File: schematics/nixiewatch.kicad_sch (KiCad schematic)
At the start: 33 parts, among them Q1 BC546, Q2 6N90C, Q3 BC546, U1 NE555P, U2 TPIC6B595, U3 MCP1702-5002E/TO, U4 TPIC6B595, U5 TPIC6B595, U6 ATtiny45V-10P

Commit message: update
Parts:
- removed C2: 330u, Capacitor_THT:CP_Radial_D8.0mm_P3.50mm, symbol Device:C_Polarized_Small
- removed C3: 100p, Capacitor_THT:C_Disc_D3.0mm_W2.0mm_P2.50mm, symbol Device:C_Small
- removed D1: 200V, Diode_THT:D_A-405_P12.70mm_Horizontal, symbol Device:D
- removed R6: 2k2, Resistor_THT:R_Axial_DIN0207_L6.3mm_D2.5mm_P7.62mm_Horizontal, symbol Device:R_Small
- added C2: 100n, Capacitor_THT:C_Disc_D3.0mm_W2.0mm_P2.50mm, symbol Device:C_Small
- added D1: 1N4007, Diode_THT:D_DO-41_SOD81_P10.16mm_Horizontal, symbol Diode:1N4007
- C4: value 4u7 400V -> 1u 200V
- Q2: value 6N90C -> BXP2N65
- R7: value 640k -> 680k
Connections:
- net +170V: now also D1.1 (K)
- net GND: now also C2.2
- net at R13.2, U2.13 (SRCK), U4.13 (SRCK)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: now also U6.3 (XTAL2/PB4); no longer U6.6 (PB1)
- net at U2.3 (SER_IN): now also U6.2 (XTAL1/PB3); no longer U6.5 (AREF/PB0)
- net at L1.2, Q2.2 (D): now also D1.2 (A)

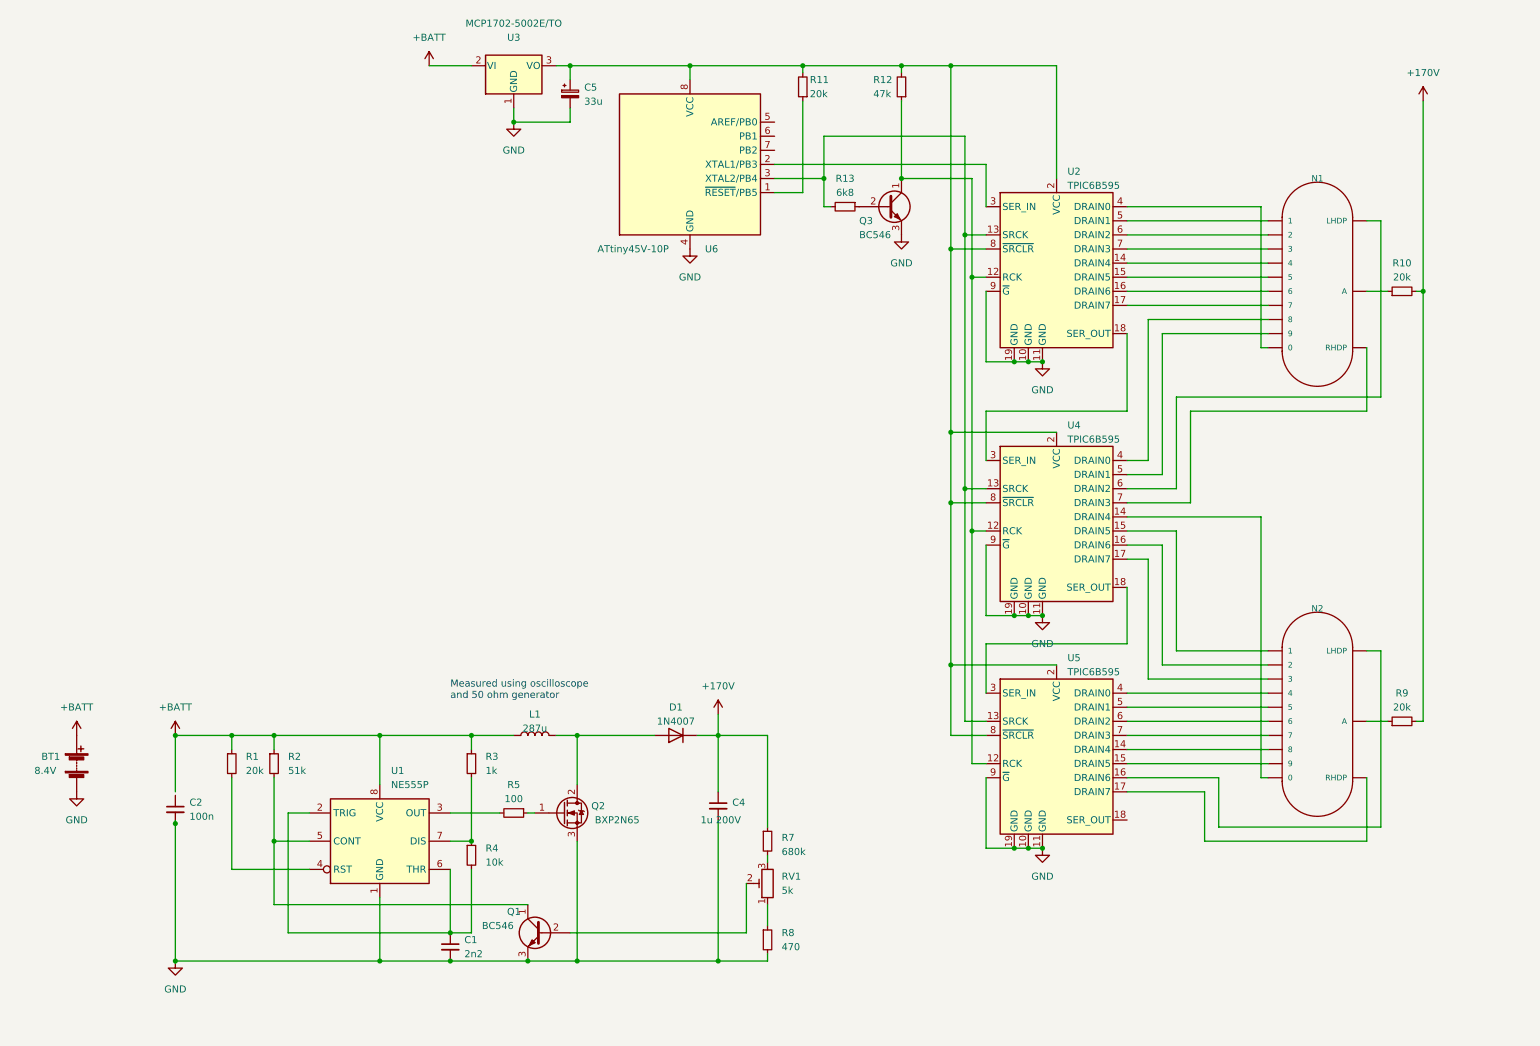
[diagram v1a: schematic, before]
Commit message: allow user to set time
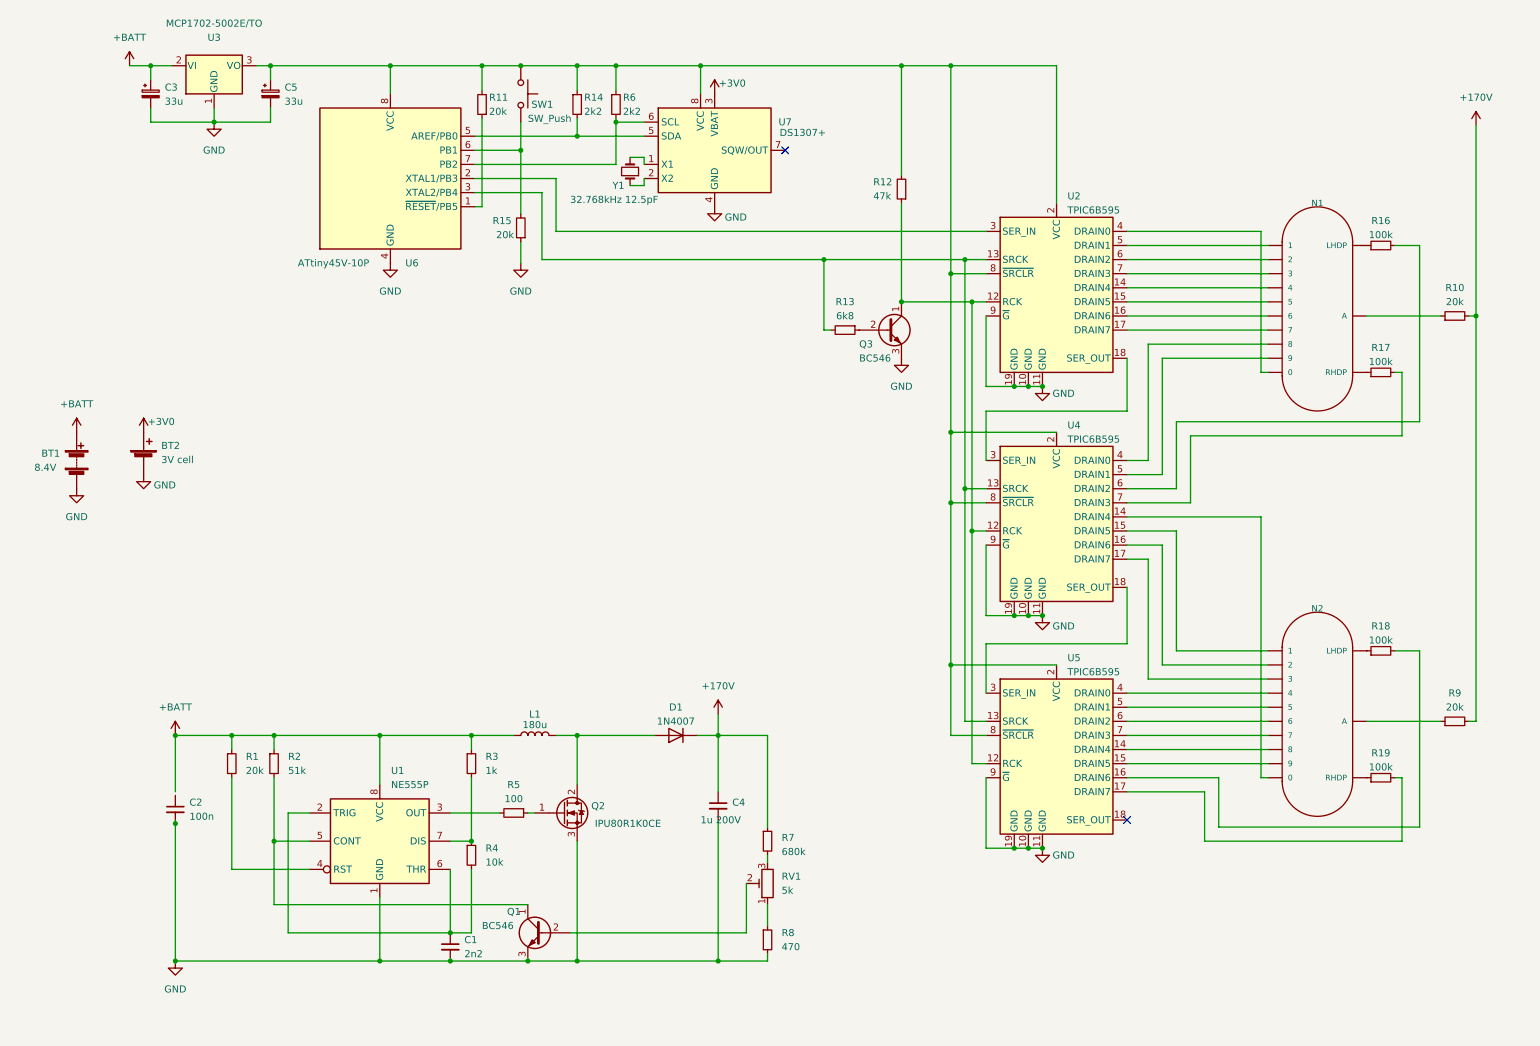
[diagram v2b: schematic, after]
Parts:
- added BT2: 3V cell, symbol Device:Battery_Cell
- added C3: 33u, symbol Device:C_Polarized_Small
- added R14, R6: 2k2, symbol Device:R_Small
- added R15: 20k, symbol Device:R_Small
- added R16, R17, R18, R19: 100k, symbol Device:R_Small
- added SW1: SW_Push, symbol Switch:SW_Push
- added U7: DS1307+, Package_DIP:DIP-8_W7.62mm, symbol Timer_RTC:DS1307+
- added Y1: 32.768kHz 12.5pF, symbol Device:Crystal_Small
- L1: value 287u -> 180u
- Q2: value BXP2N65 -> IPU80R1K0CE
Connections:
- net +BATT: now also C3.1
- net GND: now also BT2.2 (-), C3.2, R15.1, U7.4 (GND)
- net at C5.1, R11.2, R12.2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: now also R14.1, R6.1, SW1.1, U7.8 (VCC)
- net at U4.6 (DRAIN2): now also R16.2; no longer N1.LHDP
- net at U4.7 (DRAIN3): now also R17.2; no longer N1.RHDP
- net at U5.16 (DRAIN6): now also R18.2; no longer N2.LHDP
- net at U5.17 (DRAIN7): now also R19.2; no longer N2.RHDP
- net at U6.5 (AREF/PB0): now also R14.2, U7.5 (SDA)
- net at U6.6 (PB1): now also R15.2, SW1.2
- net at U6.7 (PB2): now also R6.2, U7.6 (SCL)
- new net: U7.1 (X1), Y1.2
- new net: U7.2 (X2), Y1.1
- new net: N2.LHDP, R18.1
- new net: N2.RHDP, R19.1
- new net: N1.LHDP, R16.1
- new net: N1.RHDP, R17.1
- new net +3V0: BT2.1 (+), U7.3 (VBAT)
- no-connect marks 0 -> 2
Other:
- note removed: "Measured using oscilloscope and 50 ohm generator"
- moved on the sheet: BT1, C5, N1, Q3, R10, R11, R12, R13, R9, U2, U3, U6

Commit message: pcb layout
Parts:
- BT1: footprint (none) -> Connector_PinHeader_2.00mm:PinHeader_1x01_P2.00mm_Vertical
- BT2: value 3V cell -> 3V; footprint (none) -> Connector_PinHeader_2.00mm:PinHeader_1x01_P2.00mm_Vertical
- C3, C5: footprint (none) -> Capacitor_THT:CP_Radial_D4.0mm_P1.50mm
- C4: footprint Capacitor_THT:CP_Radial_D8.0mm_P3.50mm -> Capacitor_THT:CP_Radial_D5.0mm_P2.50mm
- L1: footprint Inductor_THT:L_Toroid_Horizontal_D21.8mm_P19.60mm_Bourns_2100 -> Inductor_THT:L_Radial_D12.0mm_P5.00mm_Neosid_SD12k_style2
- N1, N2: footprint nixies-us_IN-16 -> Connector_PinHeader_2.00mm:PinHeader_1x13_P2.00mm_Vertical
- Q2: footprint Package_TO_SOT_THT:TO-220F-3_Horizontal_TabDown -> Package_TO_SOT_THT:SIPAK-1EP_Horizontal_TabDown
- R10, R11, R12, R13, R14, R15, R16, R17, R18, R19, R6, R9: footprint (none) -> Resistor_THT:R_Axial_DIN0207_L6.3mm_D2.5mm_P7.62mm_Horizontal
- SW1: footprint (none) -> Connector_Pin:Pin_D0.7mm_L6.5mm_W1.8mm_FlatFork
- U2, U4, U5: footprint (none) -> Package_DIP:DIP-20_W7.62mm
- Y1: footprint (none) -> Crystal:Crystal_C38-LF_D3.0mm_L8.0mm_Horizontal
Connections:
- net +BATT: now also C2.1
- net at U7.1 (X1): now also Y1.1; no longer Y1.2
- net at U7.2 (X2): now also Y1.2; no longer Y1.1
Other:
- moved on the sheet: Y1
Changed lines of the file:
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@@
+    (stroke (width 0) (type default))
+  )
+  (wire (pts (xy 125.095 43.18) (xy 125.095 41.91))
     (stroke (width 0) (type default))
   )
@@
     (stroke (width 0) (type default))
   )
-  (wire (pts (xy 125.095 41.91) (xy 125.095 43.18))
+  (wire (pts (xy 121.92 43.18) (xy 125.095 43.18))
     (stroke (width 0) (type default))
   )
@@
     (stroke (width 0) (type default))
   )
+  (wire (pts (xy 125.095 39.37) (xy 125.095 38.1))
+    (stroke (width 0) (type default))
+  )
   (wire (pts (xy 228.6 158.75) (xy 264.795 158.75))
     (stroke (width 0) (type default))
@@
     (stroke (width 0) (type default))
   )
-  (wire (pts (xy 122.555 38.1) (xy 125.095 38.1))
-    (stroke (width 0) (type default))
-  )
   (wire (pts (xy 113.03 34.29) (xy 125.095 34.29))
     (stroke (width 0) (type default))
@@
     (stroke (width 0) (type default))
   )
-  (wire (pts (xy 125.095 38.1) (xy 125.095 39.37))
-    (stroke (width 0) (type default))
-  )
   (wire (pts (xy 120.015 21.59) (xy 135.255 21.59))
     (stroke (width 0) (type default))
@@
     (stroke (width 0) (type default))
   )
-  (wire (pts (xy 122.555 43.18) (xy 125.095 43.18))
-    (stroke (width 0) (type default))
-  )
   (wire (pts (xy 94.615 36.83) (xy 102.87 36.83))
     (stroke (width 0) (type default))
@@
     (stroke (width 0) (type default))
   )
+  (wire (pts (xy 125.095 38.1) (xy 121.92 38.1))
+    (stroke (width 0) (type default))
+  )
   (wire (pts (xy 180.34 21.59) (xy 180.34 59.055))
     (stroke (width 0) (type default))
@@
     (stroke (width 0) (type default))
   )
-  (wire (pts (xy 40.64 142.24) (xy 40.64 152.4))
+  (wire (pts (xy 40.64 142.24) (xy 40.64 153.035))
     (stroke (width 0) (type default))
   )
@@
       (effects (font (size 1.27 1.27)) (justify left))
     )
-    (property "Footprint" "" (at 107.95 26.67 0)
+    (property "Footprint" "Connector_Pin:Pin_D0.7mm_L6.5mm_W1.8mm_FlatFork" (at 107.95 26.67 0)
       (effects (font (size 1.27 1.27)) hide)
     )
@@
       (effects (font (size 1.27 1.27)) (justify left))
     )
-    (property "Footprint" "" (at 215.9 119.38 0)
+    (property "Footprint" "Package_DIP:DIP-20_W7.62mm" (at 215.9 119.38 0)
       (effects (font (size 1.27 1.27)) hide)
     )
@@
       (effects (font (size 1.27 1.27)) (justify left))
     )
-    (property "Footprint" "" (at 215.9 161.29 0)
+    (property "Footprint" "Package_DIP:DIP-20_W7.62mm" (at 215.9 161.29 0)
       (effects (font (size 1.27 1.27)) hide)
     )
@@
       (effects (font (size 1.27 1.27)) (justify left))
     )
-    (property "Footprint" "" (at 215.9 78.105 0)
+    (property "Footprint" "Package_DIP:DIP-20_W7.62mm" (at 215.9 78.105 0)
       (effects (font (size 1.27 1.27)) hide)
     )
@@
       (effects (font (size 1.27 1.27)) (justify right))
     )
-    (property "Footprint" "" (at 95.885 28.575 0)
+    (property "Footprint" "Resistor_THT:R_Axial_DIN0207_L6.3mm_D2.5mm_P7.62mm_Horizontal" (at 95.885 28.575 0)
       (effects (font (size 1.27 1.27)) hide)
     )
@@
       (effects (font (size 1.27 1.27)) (justify left))
     )
-    (property "Footprint" "" (at 36.195 26.67 0)
+    (property "Footprint" "Capacitor_THT:CP_Radial_D4.0mm_P1.50mm" (at 36.195 26.67 0)
       (effects (font (size 1.27 1.27)) hide)
     )
@@
       (effects (font (size 1.27 1.27)))
     )
-    (property "Footprint" "" (at 271.145 66.675 0)
+    (property "Footprint" "Resistor_THT:R_Axial_DIN0207_L6.3mm_D2.5mm_P7.62mm_Horizontal" (at 271.145 66.675 0)
       (effects (font (size 1.27 1.27)) hide)
     )
@@
       (effects (font (size 1.27 1.27)) (justify left))
     )
-    (property "Footprint" "" (at 57.785 26.67 0)
+    (property "Footprint" "Capacitor_THT:CP_Radial_D4.0mm_P1.50mm" (at 57.785 26.67 0)
       (effects (font (size 1.27 1.27)) hide)
     )
@@
       (effects (font (size 1.27 1.27)) (justify left))
     )
-    (property "Value" "3V cell" (at 38.1 92.583 0)
-      (effects (font (size 1.27 1.27)) (justify left))
-    )
-    (property "Footprint" "" (at 34.925 91.186 90)
+    (property "Value" "3V" (at 38.1 92.583 0)
+      (effects (font (size 1.27 1.27)) (justify left))
+    )
+    (property "Footprint" "Connector_PinHeader_2.00mm:PinHeader_1x01_P2.00mm_Vertical" (at 34.925 91.186 90)
       (effects (font (size 1.27 1.27)) hide)
     )
@@
       (effects (font (size 1.27 1.27)))
     )
-    (property "Footprint" "" (at 257.81 127 0)
+    (property "Footprint" "Resistor_THT:R_Axial_DIN0207_L6.3mm_D2.5mm_P7.62mm_Horizontal" (at 257.81 127 0)
       (effects (font (size 1.27 1.27)) hide)
     )
@@
       (effects (font (size 1.27 1.27)))
     )
-    (property "Footprint" "" (at 257.81 149.86 0)
+    (property "Footprint" "Resistor_THT:R_Axial_DIN0207_L6.3mm_D2.5mm_P7.62mm_Horizontal" (at 257.81 149.86 0)
       (effects (font (size 1.27 1.27)) hide)
     )
@@
     )
   )
-  (symbol (lib_id "Device:Crystal_Small") (at 122.555 40.64 90) (unit 1)
-    (in_bom yes) (on_board yes) (dnp no)
-    (property "Reference" "Y1" (at 119.38 43.18 90)
+  (symbol (lib_id "Device:Crystal_Small") (at 121.92 40.64 270) (unit 1)
+    (in_bom yes) (on_board yes) (dnp no)
+    (property "Reference" "Y1" (at 121.285 43.18 90)
       (effects (font (size 1.27 1.27)) (justify right))
     )
-    (property "Value" "32.768kHz 12.5pF" (at 111.76 45.72 90)
+    (property "Value" "32.768kHz 12.5pF" (at 130.175 45.72 90)
       (effects (font (size 1.27 1.27)) (justify right))
     )
-    (property "Footprint" "" (at 122.555 40.64 0)
-      (effects (font (size 1.27 1.27)) hide)
-    )
-    (property "Datasheet" "~" (at 122.555 40.64 0)
+    (property "Footprint" "Crystal:Crystal_C38-LF_D3.0mm_L8.0mm_Horizontal" (at 121.92 40.64 0)
+      (effects (font (size 1.27 1.27)) hide)
+    )
+    (property "Datasheet" "~" (at 121.92 40.64 0)
       (effects (font (size 1.27 1.27)) hide)
     )
@@
       (effects (font (size 1.27 1.27)) (justify left))
     )
-    (property "Footprint" "" (at 22.86 91.186 90)
+    (property "Footprint" "Connector_PinHeader_2.00mm:PinHeader_1x01_P2.00mm_Vertical" (at 22.86 91.186 90)
       (effects (font (size 1.27 1.27)) hide)
     )
@@
       (effects (font (size 1.27 1.27)) (justify left))
     )
-    (property "Footprint" "Capacitor_THT:CP_Radial_D8.0mm_P3.50mm" (at 138.43 154.94 0)
+    (property "Footprint" "Capacitor_THT:CP_Radial_D5.0mm_P2.50mm" (at 138.43 154.94 0)
       (effects (font (size 1.27 1.27)) hide)
     )
@@
       (effects (font (size 1.27 1.27)) (justify left))
     )
-    (property "Footprint" "Package_TO_SOT_THT:TO-220F-3_Horizontal_TabDown" (at 115.57 153.67 0)
+    (property "Footprint" "Package_TO_SOT_THT:SIPAK-1EP_Horizontal_TabDown" (at 115.57 153.67 0)
       (effects (font (size 1.27 1.27)) hide)
     )
@@
       (effects (font (size 1.27 1.27)))
     )
-    (property "Footprint" "" (at 161.29 69.215 0)
+    (property "Footprint" "Resistor_THT:R_Axial_DIN0207_L6.3mm_D2.5mm_P7.62mm_Horizontal" (at 161.29 69.215 0)
       (effects (font (size 1.27 1.27)) hide)
     )
@@
       (effects (font (size 1.27 1.27)) (justify left))
     )
-    (property "Footprint" "" (at 120.015 28.575 0)
+    (property "Footprint" "Resistor_THT:R_Axial_DIN0207_L6.3mm_D2.5mm_P7.62mm_Horizontal" (at 120.015 28.575 0)
       (effects (font (size 1.27 1.27)) hide)
     )
@@
       (effects (font (size 1.27 1.27)))
     )
-    (property "Footprint" "Inductor_THT:L_Toroid_Horizontal_D21.8mm_P19.60mm_Bourns_2100" (at 105.41 142.24 0)
+    (property "Footprint" "Inductor_THT:L_Radial_D12.0mm_P5.00mm_Neosid_SD12k_style2" (at 105.41 142.24 0)
       (effects (font (size 1.27 1.27)) hide)
     )
@@
       (effects (font (size 1.27 1.27)))
     )
-    (property "Footprint" "" (at 257.81 53.975 0)
+    (property "Footprint" "Resistor_THT:R_Axial_DIN0207_L6.3mm_D2.5mm_P7.62mm_Horizontal" (at 257.81 53.975 0)
       (effects (font (size 1.27 1.27)) hide)
     )
@@
       (effects (font (size 1.27 1.27)) (justify right))
     )
-    (property "Footprint" "" (at 171.45 43.815 0)
+    (property "Footprint" "Resistor_THT:R_Axial_DIN0207_L6.3mm_D2.5mm_P7.62mm_Horizontal" (at 171.45 43.815 0)
       (effects (font (size 1.27 1.27)) hide)
     )
@@
       (effects (font (size 1.27 1.27)) (justify left))
     )
-    (property "Footprint" "" (at 113.03 28.575 0)
+    (property "Footprint" "Resistor_THT:R_Axial_DIN0207_L6.3mm_D2.5mm_P7.62mm_Horizontal" (at 113.03 28.575 0)
       (effects (font (size 1.27 1.27)) hide)
     )
@@
       (effects (font (size 1.27 1.27)))
     )
-    (property "Footprint" "" (at 271.145 139.7 0)
+    (property "Footprint" "Resistor_THT:R_Axial_DIN0207_L6.3mm_D2.5mm_P7.62mm_Horizontal" (at 271.145 139.7 0)
       (effects (font (size 1.27 1.27)) hide)
     )
@@
       (effects (font (size 1.143 1.143)) (justify left bottom) hide)
     )
-    (property "Footprint" "nixies-us_IN-16" (at 245.872 135.89 0)
+    (property "Footprint" "Connector_PinHeader_2.00mm:PinHeader_1x13_P2.00mm_Vertical" (at 245.872 135.89 0)
       (effects (font (size 0.508 0.508)) hide)
     )
@@
       (effects (font (size 1.27 1.27)))
     )
-    (property "Footprint" "" (at 257.81 76.835 0)
+    (property "Footprint" "Resistor_THT:R_Axial_DIN0207_L6.3mm_D2.5mm_P7.62mm_Horizontal" (at 257.81 76.835 0)
       (effects (font (size 1.27 1.27)) hide)
     )
@@
       (effects (font (size 1.143 1.143)) (justify left bottom) hide)
     )
-    (property "Footprint" "nixies-us_IN-16" (at 245.872 62.865 0)
+    (property "Footprint" "Connector_PinHeader_2.00mm:PinHeader_1x13_P2.00mm_Vertical" (at 245.872 62.865 0)
       (effects (font (size 0.508 0.508)) hide)
     )
@@
       (effects (font (size 1.27 1.27)) (justify right))
     )
-    (property "Footprint" "" (at 102.87 50.8 0)
-      (effects (font (size 1.27 1.27)) hide)
-    )
+    (property "Footprint" "Resistor_THT:R_Axial_DIN0207_L6.3mm_D2.5mm_P7.62mm_Horizontal" (at 102.87 50.8 0)
+      (effects (font (size 1.27 1.27)) hide)
+    )
